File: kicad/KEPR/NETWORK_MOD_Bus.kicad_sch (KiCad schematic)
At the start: 0 parts

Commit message: Definido os demais buses, criado folha do carimbo, versão 0.5
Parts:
- added J1: Conn_02x12_Odd_Even, symbol Connector_Generic:Conn_02x12_Odd_Even
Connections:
- new net GND: J1.1 (Pin_1), J1.2 (Pin_2)
- new net MDIO: J1.7 (Pin_7)
- new net NET_CLK_EVEN: J1.6 (Pin_6)
- new net NET_CLK_ODD: J1.5 (Pin_5)
- new net NET_CMD_EVEN: J1.12 (Pin_12), J1.14 (Pin_14), J1.16 (Pin_16), J1.22 (Pin_22), J1.8 (Pin_8)
- new net NET_CTL0_EVEN: J1.18 (Pin_18)
- new net NET_CTL0_ODD: J1.17 (Pin_17)
- new net NET_CTL1_EVEN: J1.20 (Pin_20)
- new net NET_CTL1_ODD: J1.19 (Pin_19)
- new net NET_CTL2_ODD: J1.21 (Pin_21), J1.23 (Pin_23)
- new net NET_D0_EVEN: J1.10 (Pin_10)
- new net NET_D0_ODD: J1.9 (Pin_9)
- new net NET_D1_ODD: J1.11 (Pin_11)
- new net NET_D2_ODD: J1.13 (Pin_13)
- new net NET_D3_ODD: J1.15 (Pin_15)
- new net NET_SPI_RST_N: J1.24 (Pin_24)
- new net VCC_3V3: J1.3 (Pin_3), J1.4 (Pin_4)

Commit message: Adicinado o barramento externo
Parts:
- renumbered J1 to J?

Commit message: Iniciado projeto da PCB, para uma referência de tamanho.
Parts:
- J3: renamed from J?; footprint (none) -> Connector_IDC:IDC-Header_2x25_P2.54mm_Latch6.5mm_Vertical
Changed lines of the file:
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@@
 		(on_board yes)
 		(dnp no)
-		(fields_autoplaced yes)
-		(property "Reference" "J?"
+		(property "Reference" "J3"
 			(at 201.93 105.41 0)
 			(effects
@@
 			)
 		)
-		(property "Footprint" ""
-			(at 200.66 124.46 0)
+		(property "Footprint" "Connector_IDC:IDC-Header_2x25_P2.54mm_Latch6.5mm_Vertical"
+			(at 200.66 101.6 0)
 			(effects
 				(font
 					(size 1.27 1.27)
 				)
-				(hide yes)
 			)
 		)
@@
 			(project "KEPR"
 				(path "/5d9e1dfb-5ec5-4e06-bbdb-9cbfa1c0b9f1/0260e008-78ae-4c2c-85f8-b31739d2ea08/81da33e8-b949-40cf-b6bb-f99db92e18ff"
-					(reference "J?")
+					(reference "J3")
 					(unit 1)
 				)

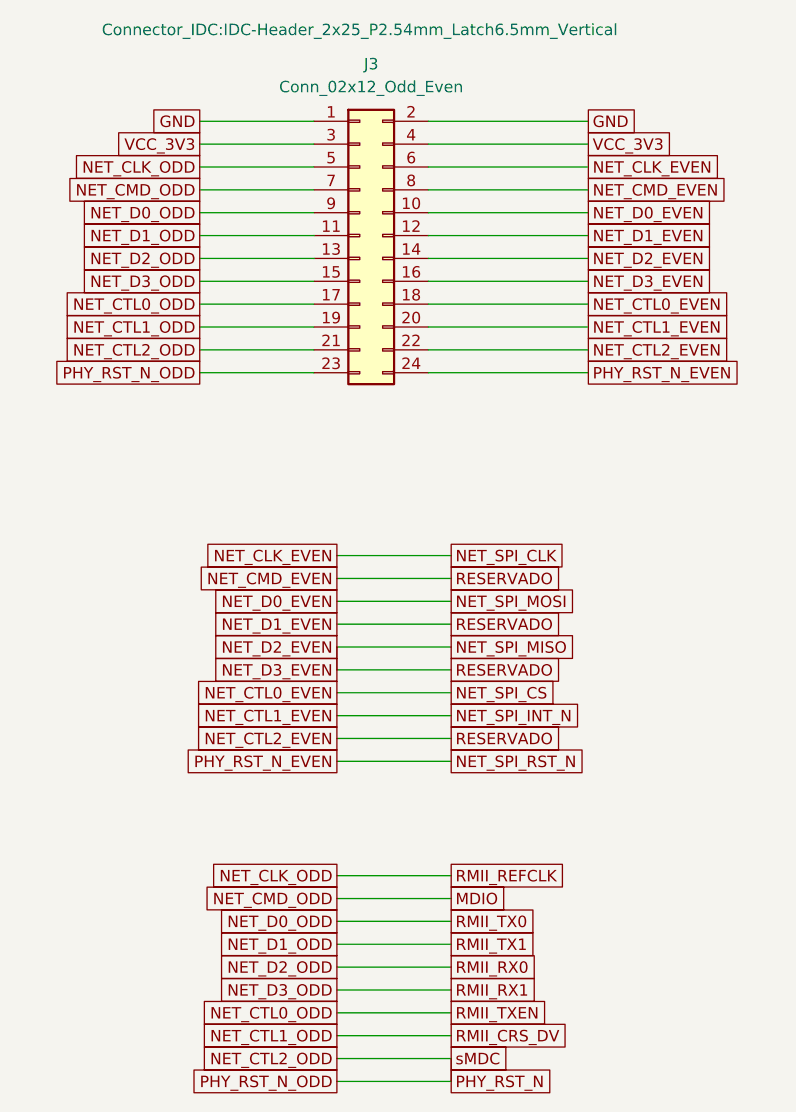
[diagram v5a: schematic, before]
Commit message: Iniciado a distribuição das vias.
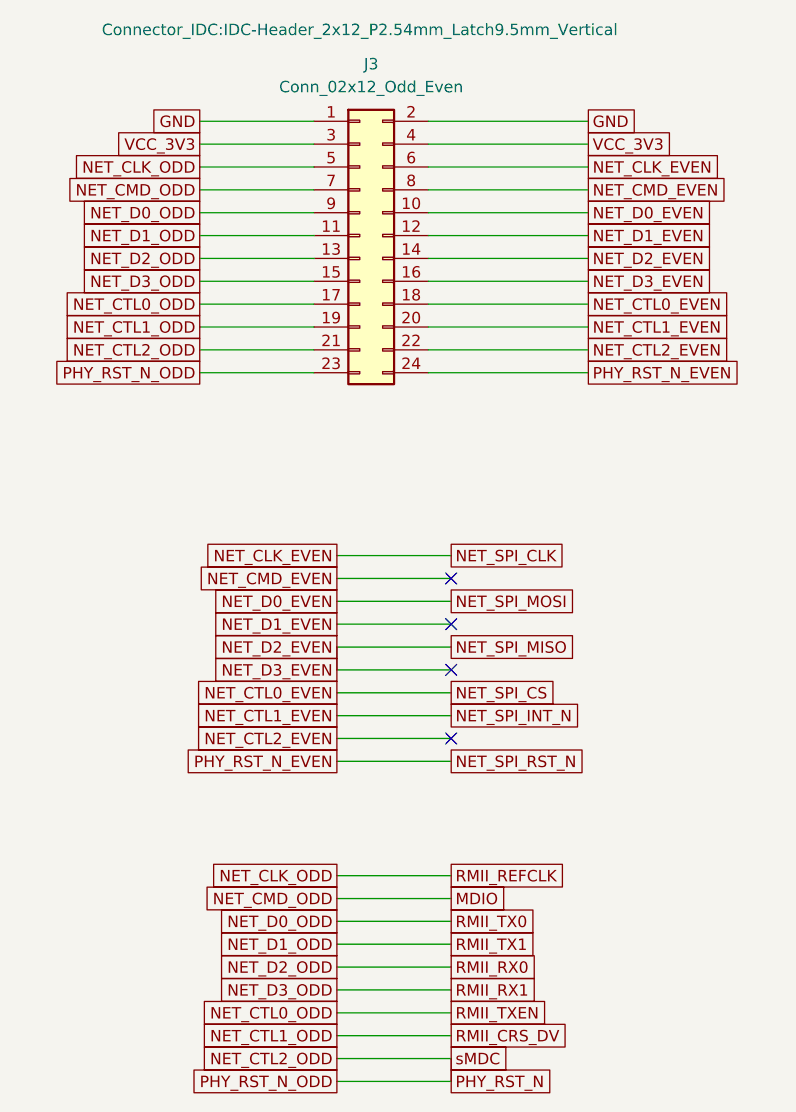
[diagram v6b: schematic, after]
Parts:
- J3: footprint Connector_IDC:IDC-Header_2x25_P2.54mm_Latch6.5mm_Vertical -> Connector_IDC:IDC-Header_2x12_P2.54mm_Latch9.5mm_Vertical
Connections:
- net NET_CMD_EVEN: no longer J3.12 (Pin_12), J3.14 (Pin_14), J3.16 (Pin_16), J3.22 (Pin_22)
- new net NET_CTL2_EVEN: J3.22 (Pin_22)
- new net NET_D1_EVEN: J3.12 (Pin_12)
- new net NET_D2_EVEN: J3.14 (Pin_14), J3.16 (Pin_16)
- no-connect marks 0 -> 4

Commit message: mais ajustes de trilha.
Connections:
- net NET_D2_EVEN: no longer J3.16 (Pin_16)
- new net NET_D3_EVEN: J3.16 (Pin_16)
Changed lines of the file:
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@@
-	(wire
-		(pts
-			(xy 198.12 172.72) (xy 198.12 170.18)
-		)
-		(stroke
-			(width 0)
-			(type default)
-		)
-	)
 	(wire
 		(pts
@@
 		(pts
 			(xy 208.28 139.7) (xy 226.06 139.7)
-		)
-		(stroke
-			(width 0)
-			(type default)
-		)
-	)
-	(wire
-		(pts
-			(xy 198.12 172.72) (xy 210.82 172.72)
 		)
 		(stroke
@@
 			)
 		)
+	)
+	(rule_area
+		(polyline
+			(pts
+				(xy 176.53 154.94) (xy 234.95 154.94) (xy 234.95 226.06) (xy 176.53 226.06)
+			)
+			(stroke
+				(width 0)
+				(type dash)
+			)
+			(fill
+				(type none)
+			)
+		)
+	)
+	(netclass_flag ""
+		(length 2.54)
+		(shape round)
+		(at 201.93 154.94 0)
+		(fields_autoplaced yes)
+		(effects
+			(font
+				(size 1.27 1.27)
+			)
+			(justify left bottom)
+		)
+		(property "Netclass" "Network"
+			(at 202.6285 152.4 0)
+			(effects
+				(font
+					(size 1.27 1.27)
+				)
+				(justify left)
+			)
+		)
+		(property "Component Class" ""
+			(at -127 1.27 0)
+			(effects
+				(font
+					(size 1.27 1.27)
+					(italic yes)
+				)
+				(justify right)
+			)
+		)
